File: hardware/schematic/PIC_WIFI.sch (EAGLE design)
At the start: 61 parts, among them J3 M40, J4 M40, J7 USB-A-S, Q1 8MHz, Q2 32.768KHz, U1 PIC32MX460F512L TQFP100, U2 3.3V, U3 5V

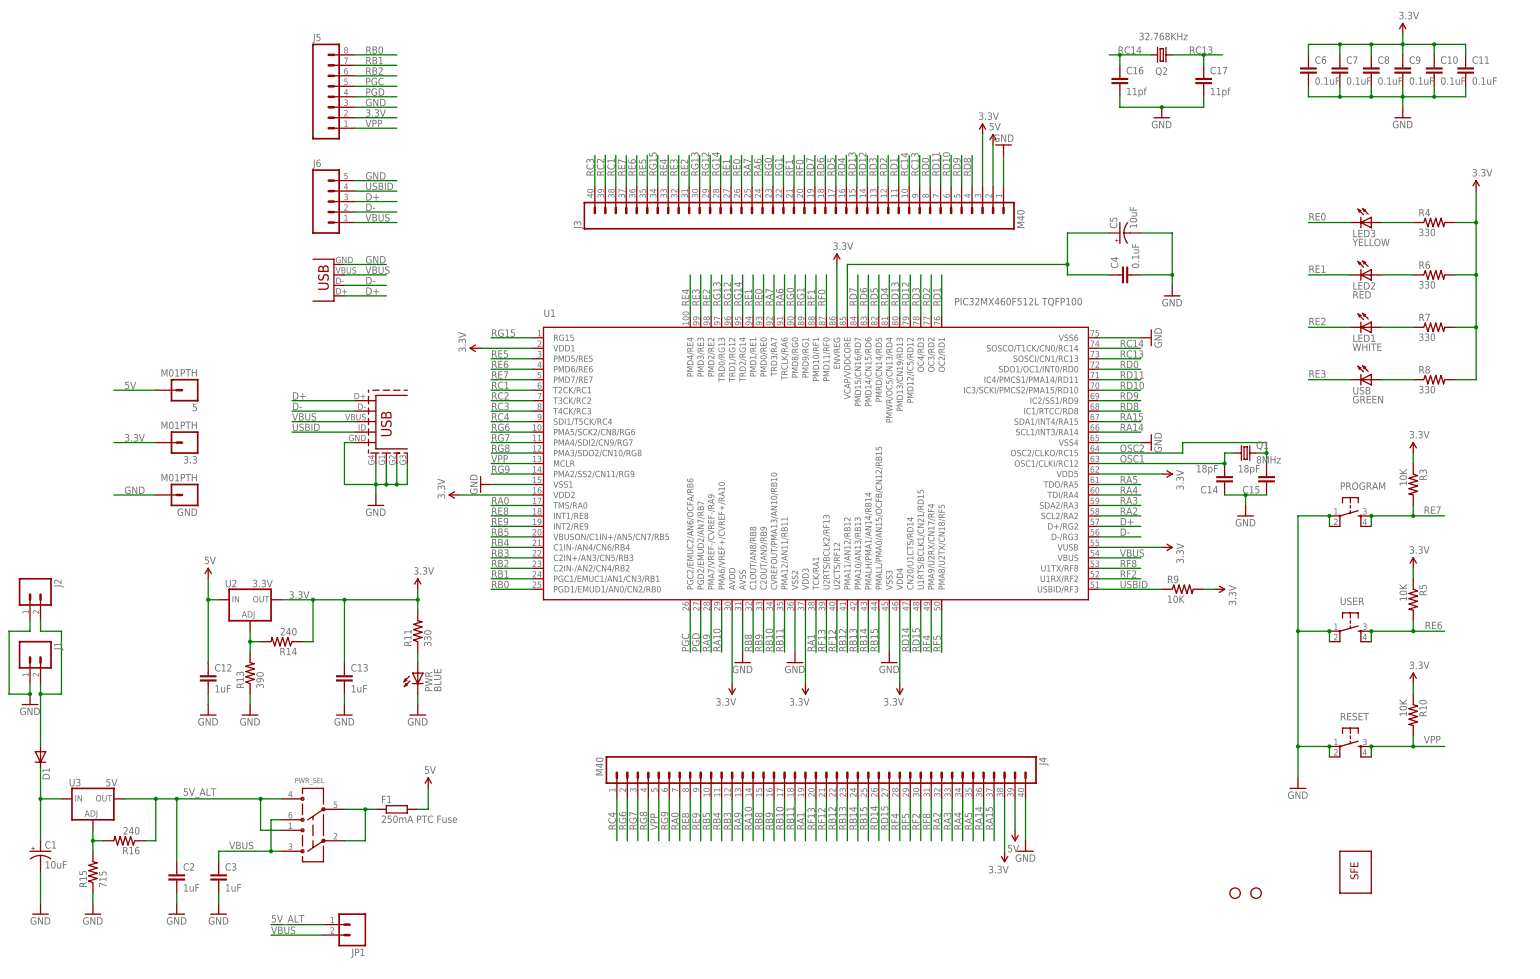
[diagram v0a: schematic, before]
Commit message: First revision of dev board.  Fixed duplicate pin in waterworx.sch
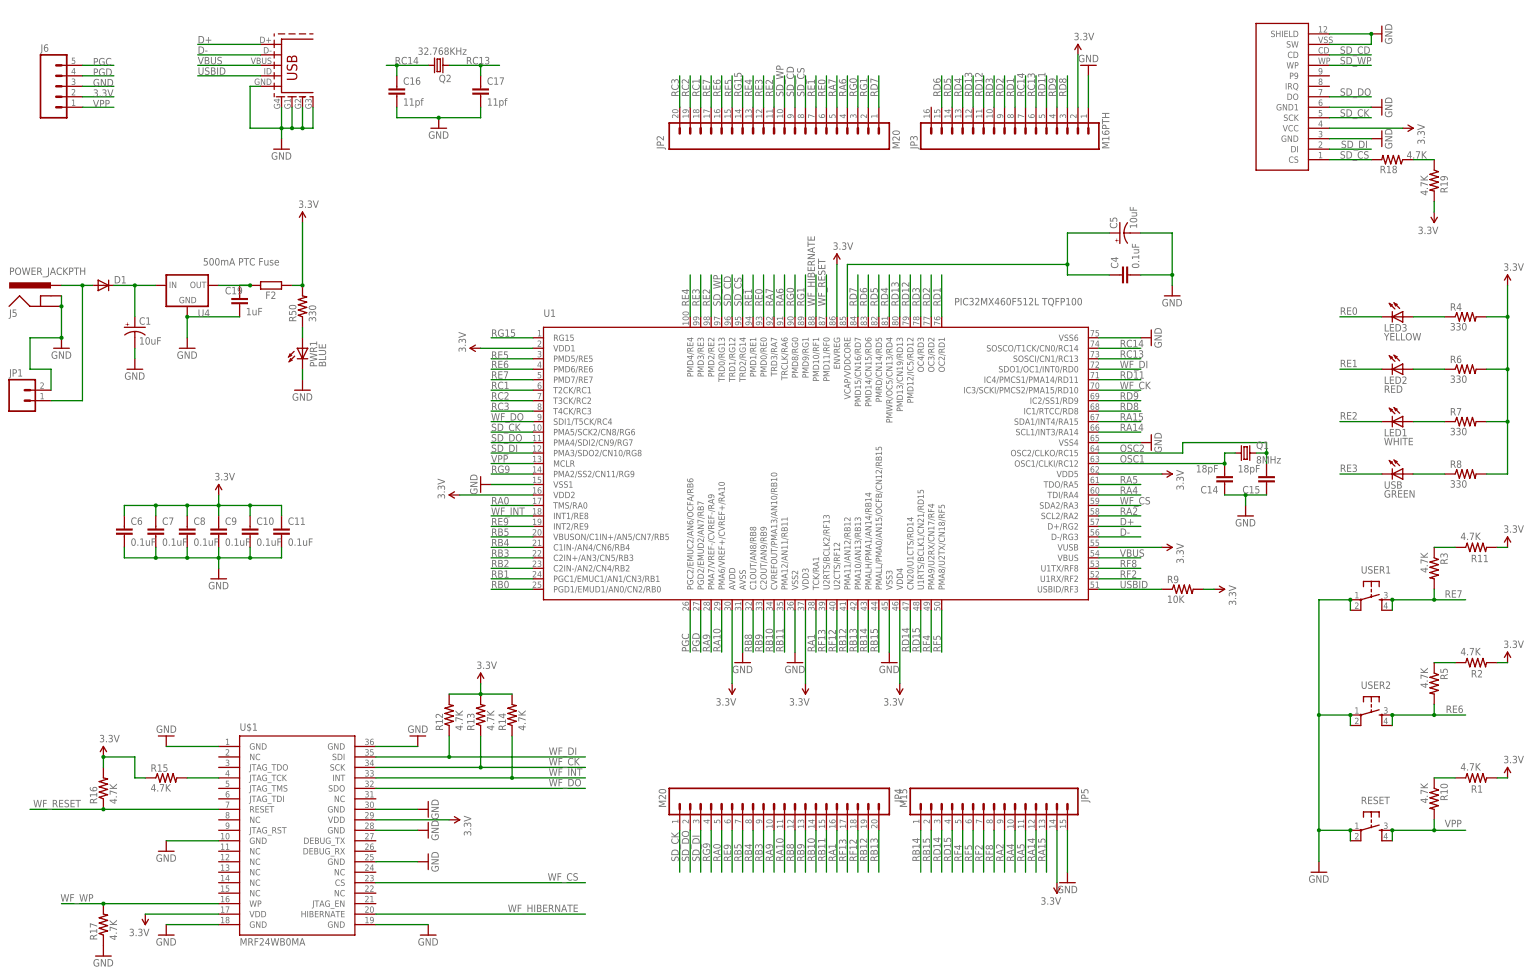
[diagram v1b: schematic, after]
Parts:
- removed 3.3, 5, GND: M01PTH, SparkFun-12-01-09:M01PTH
- removed C12, C13: 1uF, SparkFun02-20-08:CAP0402
- removed C2, C3: 1uF, SparkFun:CAP0402
- removed F1: 250mA PTC Fuse, resistor:R-EU_R1206
- removed J1: (no value), SparkFun-12-01-09:M02PTH
- removed J2: (no value), SparkFun:M02-JST-2MM-SMT
- removed J3, J4: M40, SchmalzHaus:M40
- removed J7: USB-A-S, SparkFun02-20-08:USB-A-S
- removed PROGRAM, USER: (no value), SparkFun02-20-08:TAC_SWITCHSND
- removed PWR: BLUE, SparkFun:LED0603
- removed PWR_SEL: AYZ0202, SparkFun02-20-08:AYZ0202
- removed U$4: LOGO-SFENEW, SparkFun02-20-08:LOGO-SFENEW
- removed U$6, U$7: STAND-OFF, SparkFun02-20-08:STAND-OFF
- removed U2: 3.3V, SparkFun:V_REG_317SMD
- removed U3: 5V, SparkFun:V_REG_317SMD
- added C19: 1uF, SparkFun-Passives:CAP0603-CAP
- added F2: 500mA PTC Fuse, resistor:R-EU_M1206
- added JP2, JP4: M20, SparkFun-Connectors:M20
- added JP3: M16PTH, SparkFun-Connectors:M16PTH
- added JP5: M15, SparkFun-Connectors:M15
- added PWR1: BLUE, SparkFun:LED0603
- added R1, R2: 4.7K, SparkFun:RESISTOR0402
- added R12, R17, R18, R19: 4.7K, SparkFun-Passives:RESISTOR0603-RES
- added R50: 330, SparkFun-Passives:RESISTOR0603-RES
- added U$1: MRF24WB0MA, lizardworx:MRF24WB0MA
- added U$2: SD_CARD_SOCKETALPS, lizardworx:SD_CARD_SOCKETALPS
- added U4: RECOM_X.X_REG78XX, lizardworx:RECOM_X.X_REG78XX
- added USER1, USER2: (no value), lizardworx:TAC_SWITCHB3FS
- J5: value (none) -> POWER_JACKPTH; device SchmalzHaus:M08 -> lizardworx:POWER_JACKPTH
- JP1: device SparkFun-12-01-09:M02PTH -> SparkFun-Connectors:M02PTH
- Q2: device SchmalzHaus:CRYSTAL32-SMD -> lizardworx:CRYSTAL4X2
- R10, R3, R5: value 10K -> 4.7K
- R11: value 330 -> 4.7K
- R13: value 390 -> 4.7K; device SparkFun:RESISTOR0402 -> SparkFun-Passives:RESISTOR0603-RES
- R14, R16: value 240 -> 4.7K; device SparkFun:RESISTOR0402 -> SparkFun-Passives:RESISTOR0603-RES
- R15: value 715 -> 4.7K; device SparkFun:RESISTOR0402 -> SparkFun-Passives:RESISTOR0603-RES
- RESET: device SparkFun02-20-08:TAC_SWITCHSND -> lizardworx:TAC_SWITCHB3FS
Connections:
- removed net 5V: 5.1, C12.1, F1.2, J3.2, J4.39, U2.IN
- removed net 5V_ALT: C2.1, JP1.1, PWR_SEL.3, PWR_SEL.6, R16.1, U3.OUT
- removed net N$6: PWR.A, R11.1
- removed net RA3: J4.33, U1.SDA2/RA3
- removed net RC4: J4.1, U1.SDI1/T5CK/RC4
- removed net RD0: J3.8, U1.SDO1/OC1/INT0/RD0
- removed net RD10: J3.6, U1.IC3/SCKI/PMCS2/PMA15/RD10
- removed net RE8: J4.8, U1.INT1/RE8
- removed net RF0: J3.20, U1.PMD11/RF0
- removed net RF1: J3.21, U1.PMD10/RF1
- removed net RG12: J3.29, U1.TRD1/RG12
- removed net RG13: J3.30, U1.TRD0/RG13
- removed net RG14: J3.28, U1.TRD2/RG14
- removed net RG6: J4.2, U1.PMA5/SCK2/CN8/RG6
- removed net RG7: J4.3, U1.PMA4/SDI2/CN9/RG7
- removed net RG8: J4.4, U1.PMA3/SDO2/CN10/RG8
- new net N$10: R18.1, R19.1
- new net N$19: PWR1.A, R50.1
- new net N$24: C19.1, F2.2, U4.OUT
- new net N$5: R15.2, U$1.JTAG_TCK
- new net SD_CD: JP2.9, U$2.CD, U1.TRD1/RG12
- new net SD_CK: JP4.1, U$2.SCK, U1.PMA5/SCK2/CN8/RG6
- new net SD_CS: JP2.8, R18.2, U$2.CS, U1.TRD2/RG14
- new net SD_DI: JP4.3, U$2.DI, U1.PMA3/SDO2/CN10/RG8
- new net SD_DO: JP4.2, U$2.DO, U1.PMA4/SDI2/CN9/RG7
- new net SD_WP: JP2.10, U$2.WP, U1.TRD0/RG13
- new net WF_CK: R13.1, U$1.SCK, U1.IC3/SCKI/PMCS2/PMA15/RD10
- new net WF_CS: U$1.CS, U1.SDA2/RA3
- new net WF_DI: R12.1, U$1.SDI, U1.SDO1/OC1/INT0/RD0
- new net WF_DO: U$1.SDO, U1.SDI1/T5CK/RC4
- new net WF_HIBERNATE: U$1.HIBERNATE, U1.PMD10/RF1
- new net WF_INT: R14.1, U$1.INT, U1.INT1/RE8
- new net WF_RESET: R16.1, U$1.RESET, U1.PMD11/RF0
- new net WF_WP: R17.2, U$1.WP
- net 3.3V: now also F2.1, J6.2, JP3.2, JP5.14, R1.2, R12.2, R13.2, R14.2, R15.1, R16.2, R19.2, R2.2, R50.2, U$1.VDD@17, U$1.VDD@29, U$2.VCC; no longer 3.3.1, C13.1, J3.3, J4.38, J5.2, R10.1, R14.1, R3.1, R5.1, U2.OUT
- net D+: no longer J6.3, J7.D+
- net D-: no longer J6.2, J7.D-
- net GND: now also C19.2, J5.GND, J5.GNDBREAK, J6.3, JP1.2, JP3.1, JP5.15, PWR1.C, R17.1, U$1.GND@1, U$1.GND@10, U$1.GND@18, U$1.GND@19, U$1.GND@25, U$1.GND@28, U$1.GND@30, U$1.GND@36, U$2.GND, U$2.GND1, U$2.SHIELD, U$2.SW, U4.GND, USER1.1, USER1.2, USER2.1, USER2.2; no longer C12.2, C13.2, C2.2, C3.2, GND.1, J1.1, J2.1, J3.1, J4.40, J5.3, J6.5, J7.GND, PROGRAM.1, PROGRAM.2, PWR.C, R13.1, R15.1, USER.1, USER.2
- net N$1: now also R1.1, R10.1; no longer D1.A, J1.2, J2.2
- net N$2: now also D1.A, J5.PWR, JP1.1; no longer F1.1, PWR_SEL.2, PWR_SEL.5
- net N$3: now also R2.1, R5.1; no longer R13.2, R14.2, U2.ADJ
- net N$4: now also R11.1, R3.1; no longer R15.2, R16.2, U3.ADJ
- net PGC: now also J6.5; no longer J5.5
- net PGD: now also J6.4; no longer J5.4
- net RA0: now also JP4.5; no longer J4.7
- net RA1: now also JP4.16; no longer J4.19
- net RA10: now also JP4.11; no longer J4.14
- net RA14: now also JP5.12; no longer J4.36
- net RA15: now also JP5.13; no longer J4.37
- net RA2: now also JP5.9; no longer J4.32
- net RA4: now also JP5.10; no longer J4.34
- net RA5: now also JP5.11; no longer J4.35
- net RA6: now also JP2.4; no longer J3.24
- net RA7: now also JP2.5; no longer J3.25
- net RA9: now also JP4.10; no longer J4.13
- net RB0: no longer J5.8
- net RB1: no longer J5.7
- net RB10: now also JP4.14; no longer J4.17
- net RB11: now also JP4.15; no longer J4.18
- net RB12: now also JP4.19; no longer J4.22
- net RB13: now also JP4.20; no longer J4.23
- net RB14: now also JP5.1; no longer J4.24
- net RB15: now also JP5.2; no longer J4.25
- net RB2: no longer J5.6
- net RB3: now also JP4.9; no longer J4.12
- net RB4: now also JP4.8; no longer J4.11
- net RB5: now also JP4.7; no longer J4.10
- net RB8: now also JP4.12; no longer J4.15
- net RB9: now also JP4.13; no longer J4.16
- net RC1: now also JP2.18; no longer J3.38
- net RC13: now also JP3.6, Q2.2; no longer J3.9, Q2.1
- net RC14: now also JP3.7, Q2.1; no longer J3.10, Q2.2
- net RC2: now also JP2.19; no longer J3.39
- net RC3: now also JP2.20; no longer J3.40
- net RD1: now also JP3.8; no longer J3.11
- net RD11: now also JP3.5; no longer J3.7
- net RD12: now also JP3.11; no longer J3.14
- net RD13: now also JP3.12; no longer J3.15
- net RD14: now also JP5.3; no longer J4.26
- net RD15: now also JP5.4; no longer J4.27
- net RD2: now also JP3.9; no longer J3.12
- net RD3: now also JP3.10; no longer J3.13
- net RD4: now also JP3.13; no longer J3.16
- net RD5: now also JP3.14; no longer J3.17
- net RD6: now also JP3.15; no longer J3.18
- net RD7: now also JP2.1; no longer J3.19
- net RD8: now also JP3.3; no longer J3.4
- net RD9: now also JP3.4; no longer J3.5
- net RE0: now also JP2.6; no longer J3.26
- net RE1: now also JP2.7; no longer J3.27
- net RE2: now also JP2.11; no longer J3.31
- net RE3: now also JP2.12; no longer J3.32
- net RE4: now also JP2.13; no longer J3.33
- net RE5: now also JP2.15; no longer J3.35
- net RE6: now also JP2.16, USER2.3, USER2.4; no longer J3.36, USER.3, USER.4
- net RE7: now also JP2.17, USER1.3, USER1.4; no longer J3.37, PROGRAM.3, PROGRAM.4
- net RE9: now also JP4.6; no longer J4.9
- net RF12: now also JP4.18; no longer J4.21
- net RF13: now also JP4.17; no longer J4.20
- net RF2: now also JP5.7; no longer J4.30
- net RF4: now also JP5.5; no longer J4.28
- net RF5: now also JP5.6; no longer J4.29
- net RF8: now also JP5.8; no longer J4.31
- net RG0: now also JP2.3; no longer J3.23
- net RG1: now also JP2.2; no longer J3.22
- net RG15: now also JP2.14; no longer J3.34
- net RG9: now also JP4.4; no longer J4.6
- net USBID: no longer J6.4
- net VBUS: no longer C3.1, J6.1, J7.VBUS, JP1.2, PWR_SEL.1, PWR_SEL.4
- net VIN_RAW: now also U4.IN; no longer U3.IN
- net VPP: now also J6.1; no longer J4.5, J5.1
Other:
- note added: "Alternate Supply Via Header"
- note added: "For now WP is held"
- note added: "ICSP/Debug"
- note added: "Need to supply 7.6 to 42V"
- note added: "RTC"
- note added: "SD CARD"
- note added: "WI-FI MODULE"
- note added: "WWW.HARDLYSOFTWARE.COM"
- note added: "low and not conn."
- note added: "to the PIC"
- note removed: "01/23/2010 v26 B"
- note removed: "5V to VBUS if you want to"
- note removed: "Alternate USB"
- note removed: "By: Brian Schmalz"
- note removed: "Change Log:"
- note removed: "Contact brian@schmalzhaus.com for more information."
- note removed: "ICSP/Debug/IO"
- note removed: "If you like the UBW32, please consider that"
- note removed: "J1/J2 need 7.6 to 15V"
- note removed: "J7"
- note removed: "Jumper JP1 - Short to apply"
- note removed: "MX795"
- note removed: "New for v2.6"
- note removed: "SchmalzHaus can design a customized version"
- note removed: "UBW32"
- note removed: "USB Host"
- note removed: "WWW.SCHMALZHAUS.COM/UBW32"
- note removed: "for your specific needs."
- note removed: "licenced under Creative Commons v3.0 Attribution licence"
- note removed: "use USB host functionality"
- note removed: "v2.6 Added 32KHz cyrstal pads"
- note removed: "v2.6 Changed to cyrstal from RC oscillator"
- note removed: "v2.6 Clarified port labels in schematic"
- note removed: "v2.6 D1 now 1A CDBM140-G diode"
- note removed: "v2.6 Removed pull-up resistor pads"
- note removed: "v2.6 Silk screen corrections (PortE)"
- note removed: "v2.6 Updated library to use latest SparkFun"
- note removed: "v2.6 White silk screen"
- moved on the sheet: C1, C10, C11, C16, C17, C6, C7, C8, C9, D1, J6, JP1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
